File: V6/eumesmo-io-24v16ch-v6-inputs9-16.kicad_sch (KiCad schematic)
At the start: 10 parts, among them U14 OR-3H7-4

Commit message: Renamed all files to eumesmo branding
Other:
- title: ESP 24V 16xIn/16xOut/1-Wire Module -> eumesmo 24V 16xIn/16xOut/1-Wire Module
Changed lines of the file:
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@@
 	(paper "A4")
 	(title_block
-		(title "ESP 24V 16xIn/16xOut/1-Wire Module")
-		(date "2026-02-10")
-		(rev "V6.1")
+		(title "eumesmo 24V 16xIn/16xOut/1-Wire Module")
+		(date "2026-06-13")
+		(rev "V6.2")
 	)
 	(text "I_{LED} = (24V - V_{LED}) / 10k\nI_{LED} = (24V - 2.7V) / 10k\nI_{LED} = 2,13 mA"
@@
 		)
 		(instances
-			(project "esp-24v-16ch-v6"
+			(project "eumesmo-io-24v16ch-v6"
 				(path "/2bc5a21a-1d79-419d-a592-6852cc07b00a/33bd2dd9-fdba-4639-85e9-44cc18eb8635"
 					(reference "R72")
@@
 		)
 		(instances
-			(project "esp-24v-16ch-v6"
+			(project "eumesmo-io-24v16ch-v6"
 				(path "/2bc5a21a-1d79-419d-a592-6852cc07b00a/33bd2dd9-fdba-4639-85e9-44cc18eb8635"
 					(reference "FB11")
@@
 		)
 		(instances
-			(project "esp-24v-16ch-v6"
+			(project "eumesmo-io-24v16ch-v6"
 				(path "/2bc5a21a-1d79-419d-a592-6852cc07b00a/33bd2dd9-fdba-4639-85e9-44cc18eb8635"
 					(reference "D41")
@@
 		)
 		(instances
-			(project "esp-24v-16ch-v6"
+			(project "eumesmo-io-24v16ch-v6"
 				(path "/2bc5a21a-1d79-419d-a592-6852cc07b00a/33bd2dd9-fdba-4639-85e9-44cc18eb8635"
 					(reference "#PWR0179")
@@
 		)
 		(instances
-			(project "esp-24v-16ch-v6"
+			(project "eumesmo-io-24v16ch-v6"
 				(path "/2bc5a21a-1d79-419d-a592-6852cc07b00a/33bd2dd9-fdba-4639-85e9-44cc18eb8635"
 					(reference "C58")
@@
 		)
 		(instances
-			(project "esp-24v-16ch-v6"
+			(project "eumesmo-io-24v16ch-v6"
 				(path "/2bc5a21a-1d79-419d-a592-6852cc07b00a/33bd2dd9-fdba-4639-85e9-44cc18eb8635"
 					(reference "#PWR0176")
@@
 		)
 		(instances
-			(project "esp-24v-16ch-v6"
+			(project "eumesmo-io-24v16ch-v6"
 				(path "/2bc5a21a-1d79-419d-a592-6852cc07b00a/33bd2dd9-fdba-4639-85e9-44cc18eb8635"
 					(reference "#PWR0178")
@@
 		)
 		(instances
-			(project "esp-24v-16ch-v6"
+			(project "eumesmo-io-24v16ch-v6"
 				(path "/2bc5a21a-1d79-419d-a592-6852cc07b00a/33bd2dd9-fdba-4639-85e9-44cc18eb8635"
 					(reference "D42")
@@
 		)
 		(instances
-			(project "esp-24v-16ch-v6"
+			(project "eumesmo-io-24v16ch-v6"
 				(path "/2bc5a21a-1d79-419d-a592-6852cc07b00a/33bd2dd9-fdba-4639-85e9-44cc18eb8635"
 					(reference "D40")
@@
 		)
 		(instances
-			(project "esp-24v-16ch-v6"
+			(project "eumesmo-io-24v16ch-v6"
 				(path "/2bc5a21a-1d79-419d-a592-6852cc07b00a/33bd2dd9-fdba-4639-85e9-44cc18eb8635"
 					(reference "#PWR0173")
@@
 		)
 		(instances
-			(project "esp-24v-16ch-v6"
+			(project "eumesmo-io-24v16ch-v6"
 				(path "/2bc5a21a-1d79-419d-a592-6852cc07b00a/33bd2dd9-fdba-4639-85e9-44cc18eb8635"
 					(reference "R71")
@@
 		)
 		(instances
-			(project "esp-24v-16ch-v6"
+			(project "eumesmo-io-24v16ch-v6"
 				(path "/2bc5a21a-1d79-419d-a592-6852cc07b00a/33bd2dd9-fdba-4639-85e9-44cc18eb8635"
 					(reference "#PWR0174")
@@
 		)
 		(instances
-			(project "esp-24v-16ch-v6"
+			(project "eumesmo-io-24v16ch-v6"
 				(path "/2bc5a21a-1d79-419d-a592-6852cc07b00a/33bd2dd9-fdba-4639-85e9-44cc18eb8635"
 					(reference "#PWR0177")
@@
 		)
 		(instances
-			(project "esp-24v-16ch-v6"
+			(project "eumesmo-io-24v16ch-v6"
 				(path "/2bc5a21a-1d79-419d-a592-6852cc07b00a/33bd2dd9-fdba-4639-85e9-44cc18eb8635"
 					(reference "C57")
@@
 		)
 		(instances
-			(project "esp-24v-16ch-v6"
+			(project "eumesmo-io-24v16ch-v6"
 				(path "/2bc5a21a-1d79-419d-a592-6852cc07b00a/33bd2dd9-fdba-4639-85e9-44cc18eb8635"
 					(reference "#PWR0175")
@@
 		)
 		(instances
-			(project "esp-24v-16ch-v6"
+			(project "eumesmo-io-24v16ch-v6"
 				(path "/2bc5a21a-1d79-419d-a592-6852cc07b00a/33bd2dd9-fdba-4639-85e9-44cc18eb8635"
 					(reference "U14")
@@
 		)
 		(instances
-			(project "esp-24v-16ch-v6"
+			(project "eumesmo-io-24v16ch-v6"
 				(path "/2bc5a21a-1d79-419d-a592-6852cc07b00a/33bd2dd9-fdba-4639-85e9-44cc18eb8635"
 					(reference "R73")

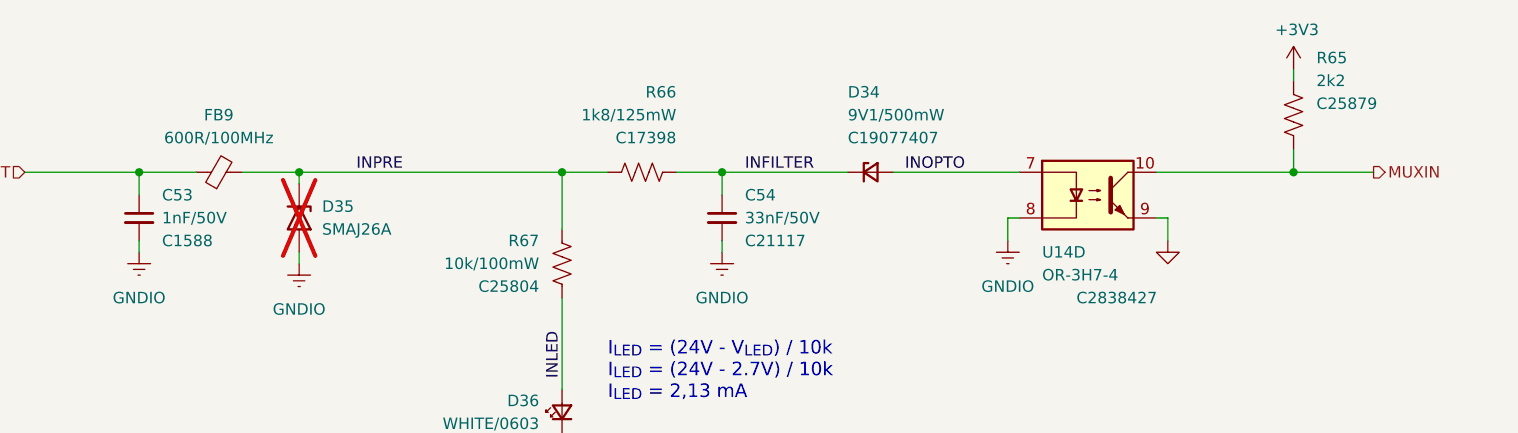
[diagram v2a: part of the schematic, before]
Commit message: Added CPU health LED
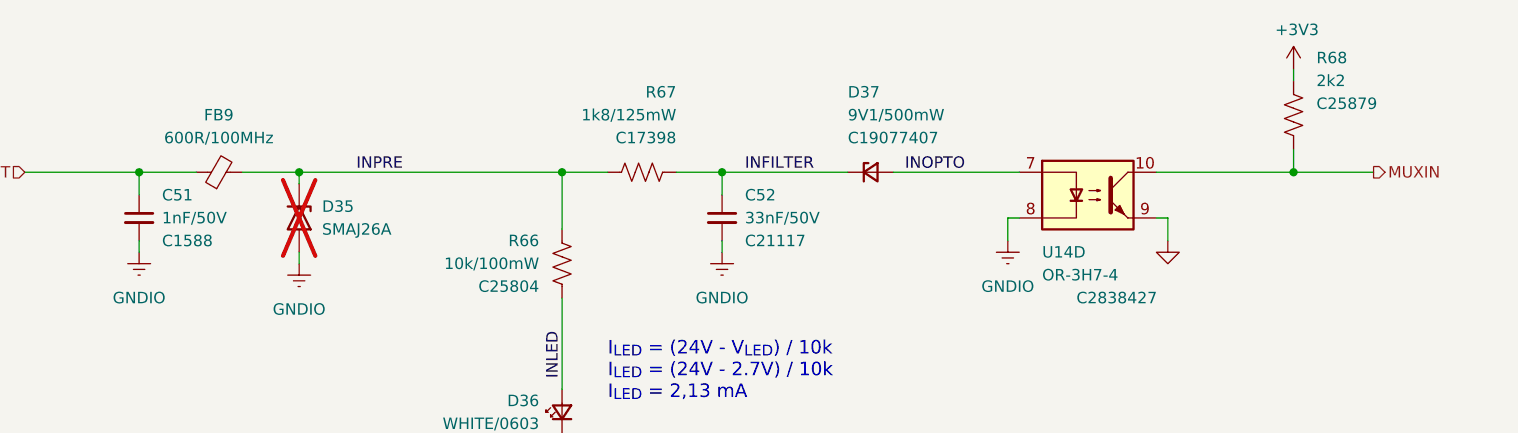
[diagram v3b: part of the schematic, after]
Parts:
- renumbered C53 to C51, C54 to C52, D34 to D37, R67 to R66, R66 to R67, R65 to R68
